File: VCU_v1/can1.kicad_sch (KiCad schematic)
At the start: 4 parts, among them U11 MCP2562 E/SN

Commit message: p dih r
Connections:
- net CAN1_L: no longer JP2.1 (A)
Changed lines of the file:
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@@
-		(color 0 0 0 0)
-	)
-	(junction
-		(at 227.33 88.9)
-		(diameter 0)
 		(color 0 0 0 0)
 	)
@@
 		(pts
 			(xy 187.96 88.9) (xy 204.47 88.9)
-		)
-		(stroke
-			(width 0)
-			(type default)
-		)
-	)
-	(wire
-		(pts
-			(xy 204.47 67.31) (xy 204.47 64.77)
 		)
 		(stroke
@@
 	(wire
 		(pts
-			(xy 227.33 88.9) (xy 228.6 88.9)
+			(xy 204.47 88.9) (xy 215.9 88.9)
 		)
 		(stroke
@@
 		(pts
 			(xy 152.4 85.09) (xy 157.48 85.09)
-		)
-		(stroke
-			(width 0)
-			(type default)
-		)
-	)
-	(wire
-		(pts
-			(xy 204.47 64.77) (xy 227.33 64.77)
-		)
-		(stroke
-			(width 0)
-			(type default)
-		)
-	)
-	(wire
-		(pts
-			(xy 204.47 88.9) (xy 227.33 88.9)
 		)
 		(stroke
@@
 	(wire
 		(pts
-			(xy 191.77 69.85) (xy 191.77 73.66)
+			(xy 191.77 63.5) (xy 191.77 73.66)
 		)
 		(stroke
@@
 	(wire
 		(pts
-			(xy 227.33 64.77) (xy 227.33 88.9)
-		)
-		(stroke
-			(width 0)
-			(type default)
-		)
-	)
-	(wire
-		(pts
 			(xy 123.19 73.66) (xy 124.46 73.66)
 		)
@@
 	(hierarchical_label "CAN1_L"
 		(shape input)
-		(at 228.6 88.9 0)
+		(at 215.9 88.9 0)
 		(effects
 			(font
@@
 	(hierarchical_label "CAN1_H"
 		(shape input)
-		(at 191.77 69.85 90)
+		(at 191.77 63.5 0)
 		(effects
 			(font

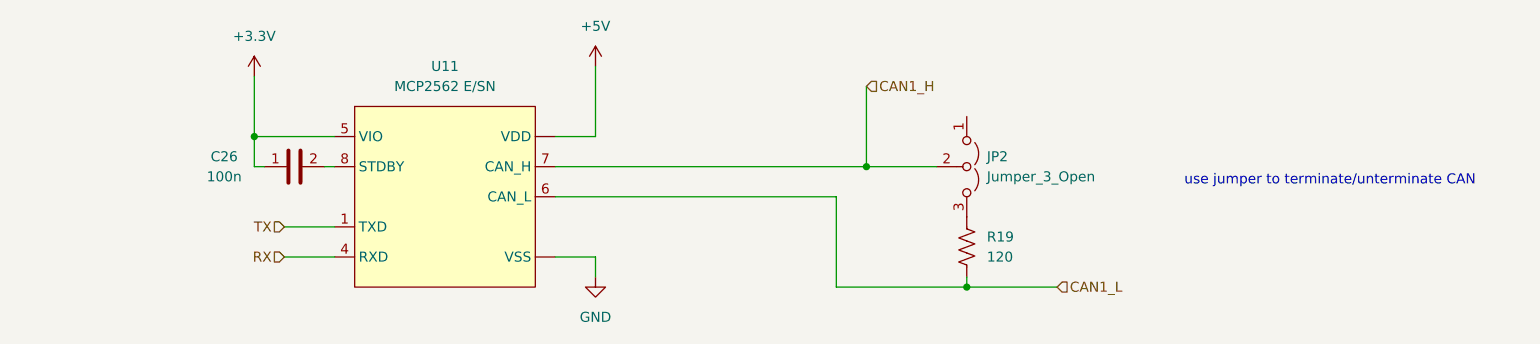
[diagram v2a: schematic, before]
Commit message: v1 schematic (actually) complete, let the layout commence
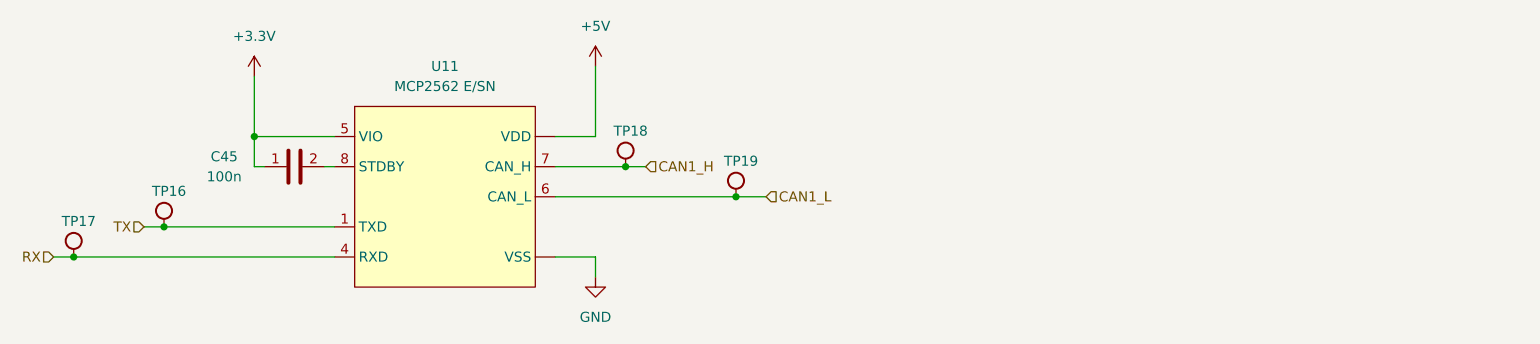
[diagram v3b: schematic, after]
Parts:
- removed JP2: Jumper_3_Open, symbol Jumper:Jumper_3_Open
- removed R19: 120, Resistor_SMD:R_0603_1608Metric_Pad0.98x0.95mm_HandSolder, symbol BFR Resistors:RMCF0603FT120R
- added TP16, TP17, TP18, TP19: RH-5015, TestPoint:TestPoint_Keystone_5015_Micro_Mini, symbol .Test-Point:RH-5015
- U11: footprint (none) -> Package_SO:SOIC-8_3.9x4.9mm_P1.27mm
- renumbered C26 to C45
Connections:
- net CAN1_H: now also TP18.1
- net CAN1_L: now also TP19.1
- net RX: now also TP17.1
- net TX: now also TP16.1
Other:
- note removed: "use jumper to terminate/unterminate CAN"

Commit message: begin pcb design
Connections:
- net +5V: now also U11.3 (VDD); no longer U11. (VSS)
- net GND: now also U11.2 (VSS); no longer U11. (VSS)
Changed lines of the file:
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@@
 		(pin "4"
 		)
-		(pin ""
+		(pin "2"
 		)
 		(pin "7"
@@
 		(pin "6"
 		)
-		(pin ""
+		(pin "3"
 		)
 		(instances

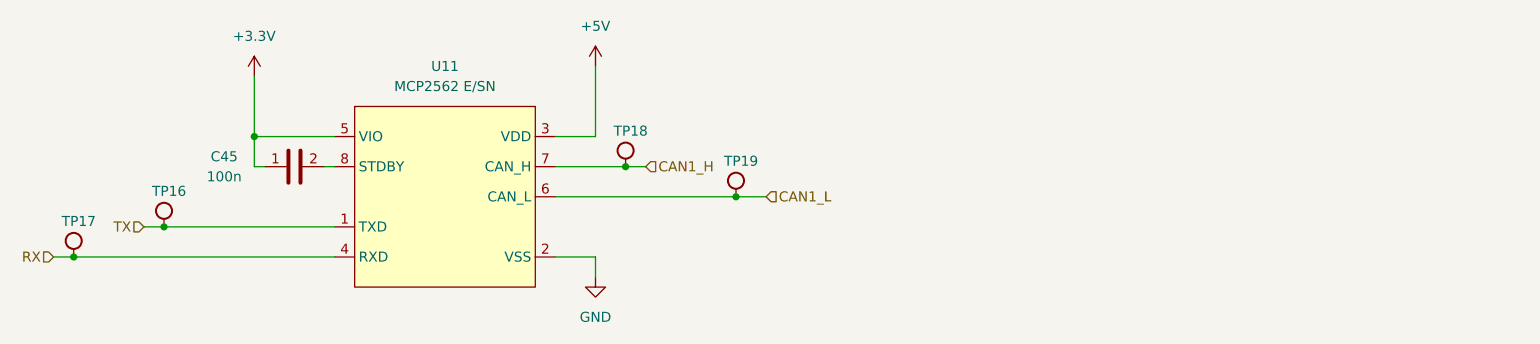
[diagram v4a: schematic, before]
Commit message: vcu placements complete
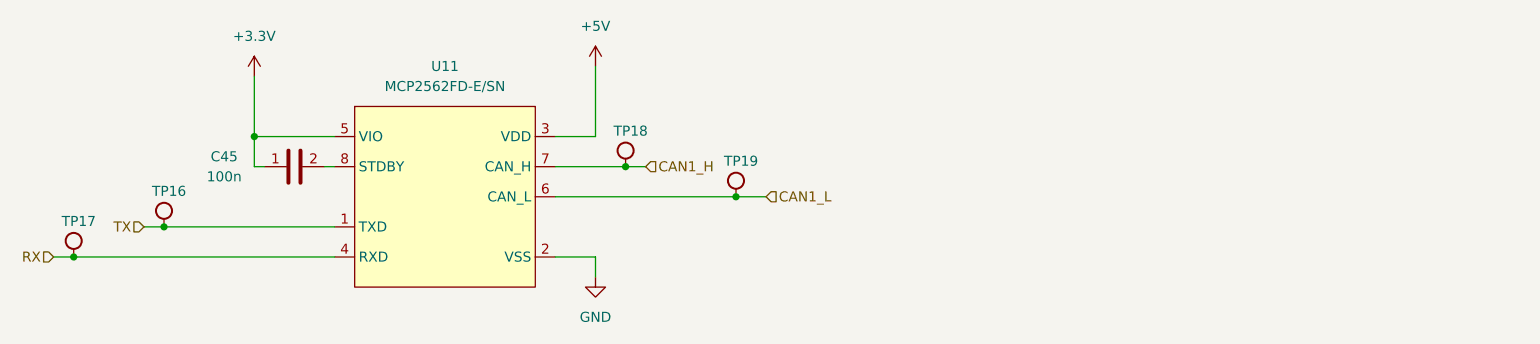
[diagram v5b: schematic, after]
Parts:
- U11: value MCP2562 E/SN -> MCP2562FD-E/SN; LCSC P/N C53609 -> C124016; Mouser P/N 579-MCP2562-E/SN -> 579-MCP2562FD-E/SN
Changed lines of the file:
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@@
 			)
 		)
-		(property "Value" "MCP2562 E/SN"
+		(property "Value" "MCP2562FD-E/SN"
 			(at 138.43 63.5 0)
 			(effects
@@
 			)
 		)
-		(property "Datasheet" "https://www.mouser.com/datasheet/2/268/20005167C-3443186.pdf"
+		(property "Datasheet" "https://ww1.microchip.com/downloads/en/DeviceDoc/20005284A.pdf"
 			(at 138.43 62.23 0)
 			(effects
@@
 			)
 		)
-		(property "Mouser P/N" "579-MCP2562-E/SN "
+		(property "Mouser P/N" "579-MCP2562FD-E/SN "
 			(at 138.43 62.23 0)
 			(effects
@@
 			)
 		)
-		(property "LCSC P/N" "C53609"
+		(property "LCSC P/N" " C124016"
 			(at 138.43 62.23 0)
 			(effects

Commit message: almost done i promise
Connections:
- net GND: now also C45.2, U11.8 (STDBY)
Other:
- moved on the sheet: C45, TP16, TP17
